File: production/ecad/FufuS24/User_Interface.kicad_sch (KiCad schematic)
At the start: 20 parts, among them J3 HDMI_A, J4 USB_B_Micro

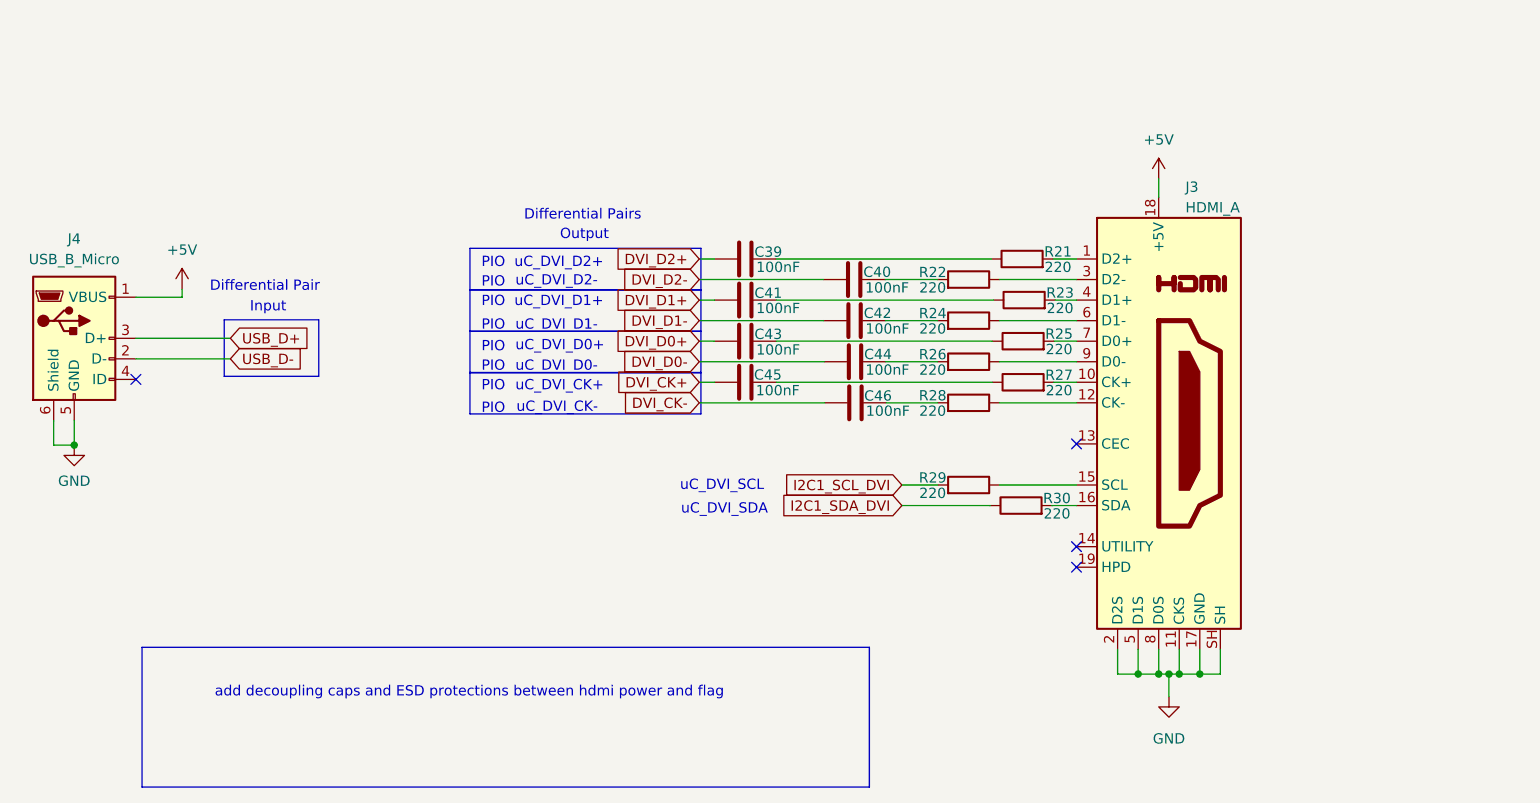
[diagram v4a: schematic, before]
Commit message: Added ESD diodes to UI schem
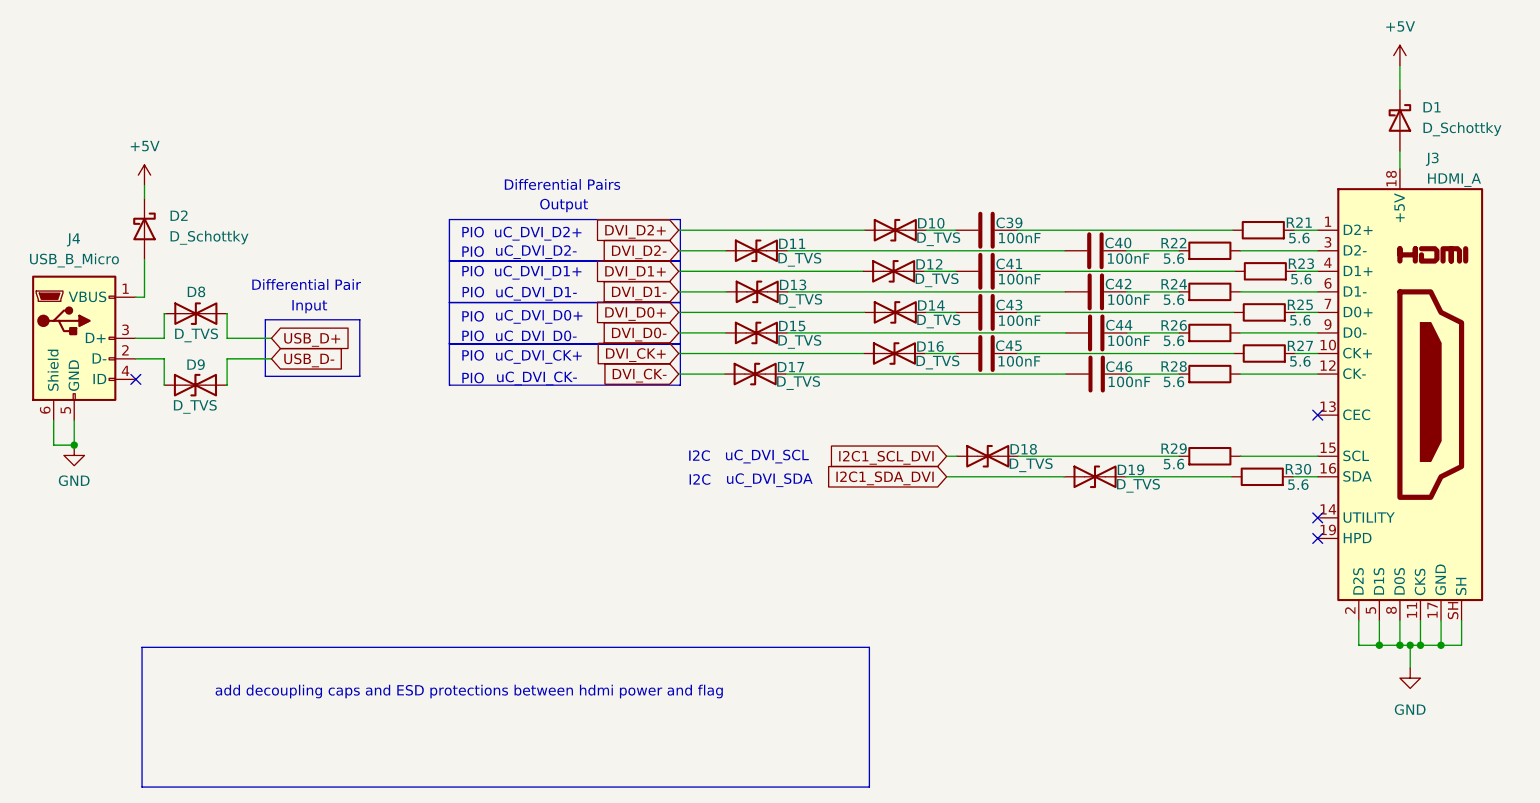
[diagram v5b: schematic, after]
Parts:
- added D1, D2: D_Schottky, symbol Device:D_Schottky
- added D10, D11, D12, D13, D14, D15, D16, D17, D18, D19, D8, D9: D_TVS, symbol Device:D_TVS
- R21, R22, R23, R24, R25, R26, R27, R28, R29, R30: value 220 -> 5.6
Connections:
- net +5V: now also D1.1 (K), D2.1 (K); no longer J3.18 (+5V), J4.1 (VBUS)
- net DVI_CK+: now also D16.1 (A1); no longer C45.1
- net DVI_CK-: now also D17.1 (A1); no longer C46.1
- net DVI_D0+: now also D14.1 (A1); no longer C43.1
- net DVI_D0-: now also D15.1 (A1); no longer C44.1
- net DVI_D1+: now also D12.1 (A1); no longer C41.1
- net DVI_D1-: now also D13.1 (A1); no longer C42.1
- net DVI_D2+: now also D10.1 (A1); no longer C39.1
- net DVI_D2-: now also D11.1 (A1); no longer C40.1
- net I2C1_SCL_DVI: now also D18.1 (A1); no longer R29.2
- net I2C1_SDA_DVI: now also D19.1 (A1); no longer R30.1
- net USB_D+: now also D8.2 (A2); no longer J4.3 (D+)
- net USB_D-: now also D9.2 (A2); no longer J4.2 (D-)
- new net: C45.1, D16.2 (A2)
- new net: C39.1, D10.2 (A2)
- new net: C41.1, D12.2 (A2)
- new net: C40.1, D11.2 (A2)
- new net: D9.1 (A1), J4.2 (D-)
- new net: D2.2 (A), J4.1 (VBUS)
- new net: D8.1 (A1), J4.3 (D+)
- new net: C44.1, D15.2 (A2)
- new net: D18.2 (A2), R29.2
- new net: C42.1, D13.2 (A2)
- new net: D1.2 (A), J3.18 (+5V)
- new net: C46.1, D17.2 (A2)
- new net: D19.2 (A2), R30.1
- new net: C43.1, D14.2 (A2)
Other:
- note added: "I2C"
- moved on the sheet: C39, C40, C41, C42, C43, C44, C45, C46, J3, R21, R22, R23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

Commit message: added ESD and diodes but idk if correctly done
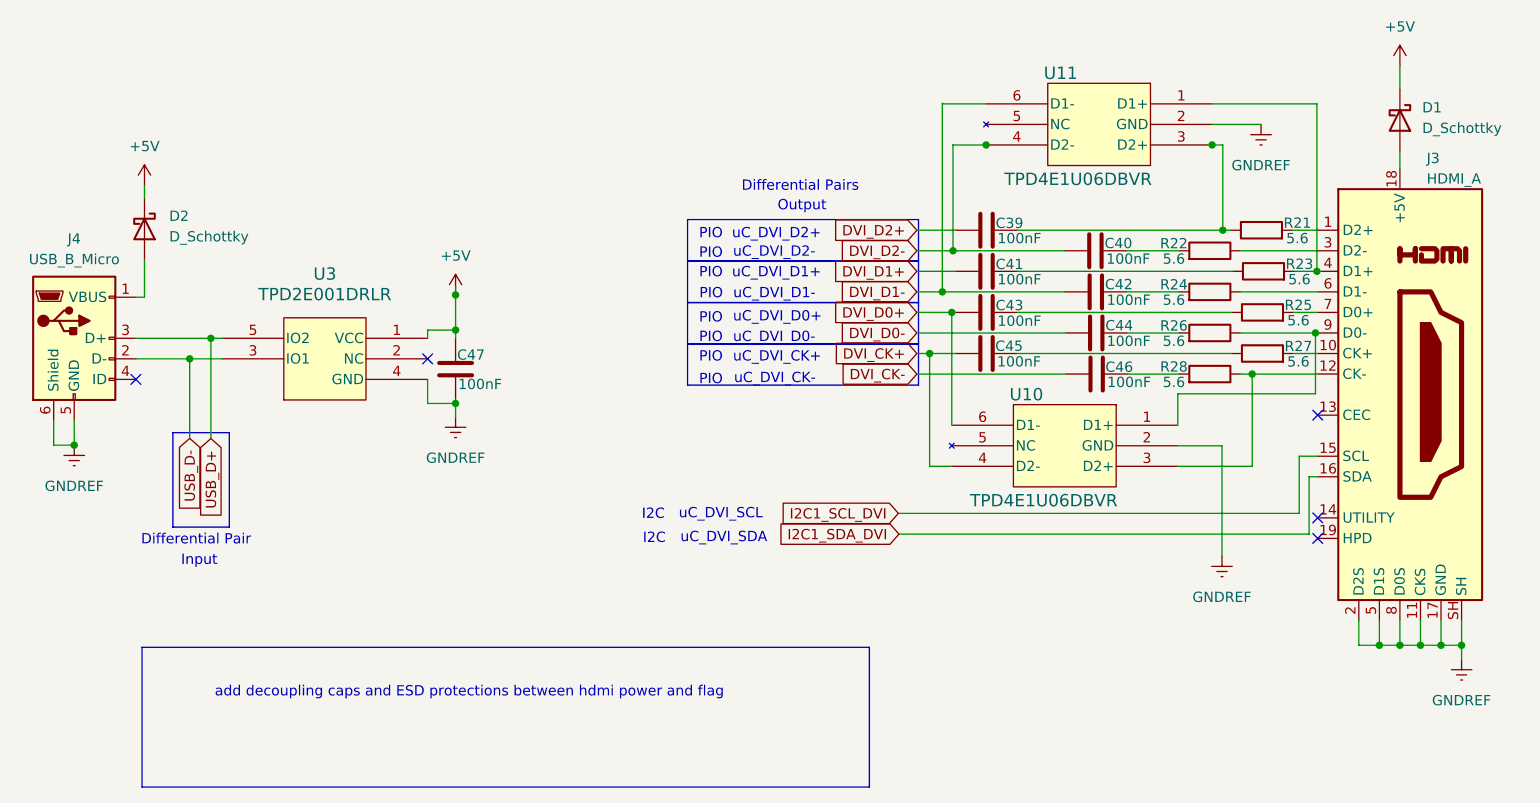
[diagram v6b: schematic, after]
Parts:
- removed D10, D11, D12, D13, D14, D15, D16, D17, D18, D19, D8, D9: D_TVS, symbol Device:D_TVS
- removed R29, R30: 5.6, symbol Device:R
- added C47: 100nF, symbol Device:C
- added U10, U11: TPD4E1U06DBVR, DBV6_TEX, symbol TPD4E1U06DBVR:TPD4E1U06DBVR
- added U3: TPD2E001DRLR, DRL5, symbol TPD2E001DRLR:TPD2E001DRLR
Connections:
- net +5V: now also C47.2, U3.1 (VCC)
- net DVI_CK+: now also C45.1, U10.4 (D2-)
- net DVI_CK-: now also C46.1
- net DVI_D0+: now also C43.1, U10.6 (D1-)
- net DVI_D0-: now also C44.1
- net DVI_D1+: now also C41.1
- net DVI_D1-: now also C42.1, U11.6 (D1-)
- net DVI_D2+: now also C39.1
- net DVI_D2-: now also C40.1, U11.4 (D2-)
- net I2C1_SCL_DVI: now also J3.15 (SCL)
- net I2C1_SDA_DVI: now also J3.16 (SDA)
- net USB_D+: now also J4.3 (D+), U3.5 (IO2)
- net USB_D-: now also J4.2 (D-), U3.3 (IO1)
- net at C39.2, R21.1: now also U11.3 (D2+)
- net at J3.12 (CK-), R28.1: now also U10.3 (D2+)
- net at J3.4 (D1+), R23.2: now also U11.1 (D1+)
- net at J3.9 (D0-), R26.1: now also U10.1 (D1+)
- net GND renamed GNDREF
- net GNDREF: now also C47.1, U10.2 (GND), U11.2 (GND), U3.4 (GND)
- no-connect marks 4 -> 5

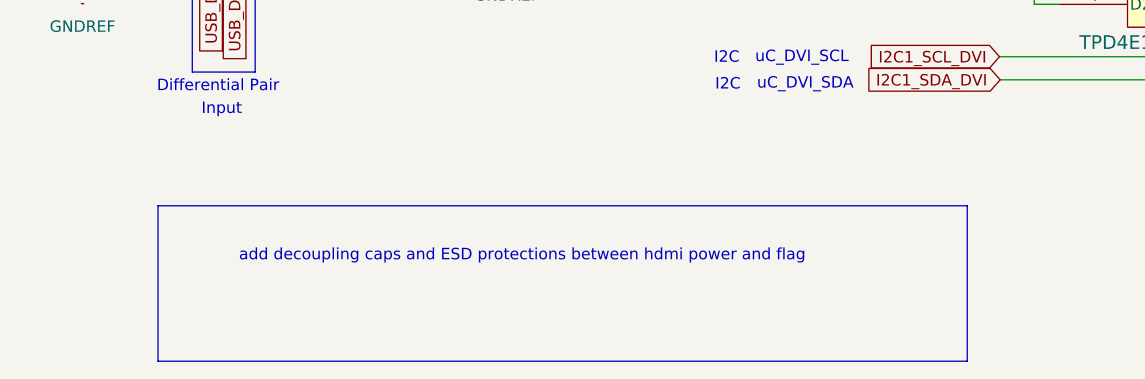
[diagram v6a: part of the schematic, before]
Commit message: removed notes from UI schem
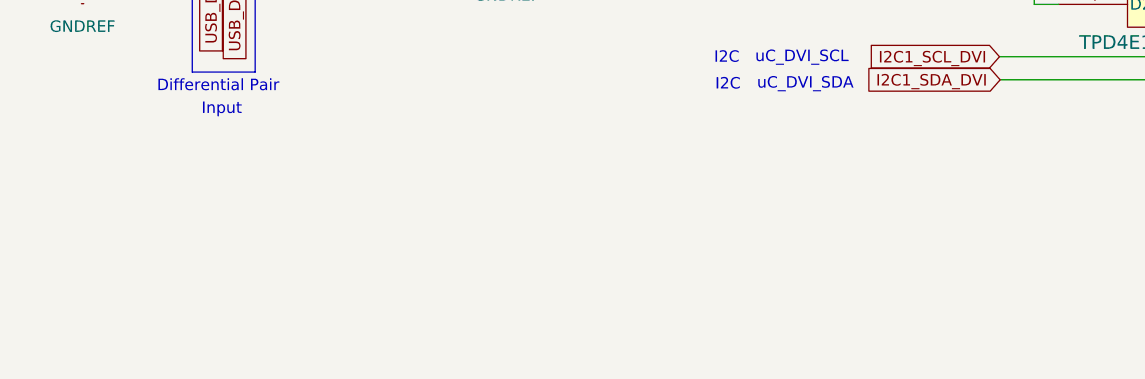
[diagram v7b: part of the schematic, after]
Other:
- note removed: "add decoupling caps and ESD protections between hdmi power and flag"
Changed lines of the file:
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@@
-    (fill (type none))
-  )
-  (rectangle (start 93.0656 107.0864) (end 182.9816 124.3584)
-    (stroke (width 0) (type default))
     (fill (type none))
   )
@@
     (effects (font (size 1.27 1.27) (color 238 64 255 1)) (justify left bottom))
   )
-  (text "add decoupling caps and ESD protections between hdmi power and flag"
-    (at 102.0572 113.4364 0)
-    (effects (font (size 1.27 1.27) (color 0 0 0 1)) (justify left bottom))
-  )
   (text "Input\n" (at 97.8916 97.1804 0)

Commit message: efan 3
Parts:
- C39, C40, C41, C42, C43, C44, C45, C46, C47: footprint (none) -> footprints:CAPC2012X94N
- R21, R22, R23, R24, R25, R26, R27, R28: footprint (none) -> footprints:RESC2012X60N
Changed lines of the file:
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@@
       (effects (font (size 1.27 1.27)))
     )
-    (property "Footprint" "" (at 231.5718 72.5424 90)
+    (property "Footprint" "footprints:RESC2012X60N" (at 231.5718 72.5424 90)
       (effects (font (size 1.27 1.27)) hide)
     )
@@
       (effects (font (size 1.27 1.27)))
     )
-    (property "Footprint" "" (at 130.8608 68.8848 0)
+    (property "Footprint" "footprints:CAPC2012X94N" (at 130.8608 68.8848 0)
       (effects (font (size 1.27 1.27)) hide)
     )
@@
       (effects (font (size 1.27 1.27)))
     )
-    (property "Footprint" "" (at 201.2696 69.7992 0)
+    (property "Footprint" "footprints:CAPC2012X94N" (at 201.2696 69.7992 0)
       (effects (font (size 1.27 1.27)) hide)
     )
@@
       (effects (font (size 1.27 1.27)))
     )
-    (property "Footprint" "" (at 214.7316 57.0992 0)
+    (property "Footprint" "footprints:CAPC2012X94N" (at 214.7316 57.0992 0)
       (effects (font (size 1.27 1.27)) hide)
     )
@@
       (effects (font (size 1.27 1.27)))
     )
-    (property "Footprint" "" (at 225.0694 59.8424 90)
+    (property "Footprint" "footprints:RESC2012X60N" (at 225.0694 59.8424 90)
       (effects (font (size 1.27 1.27)) hide)
     )
@@
       (effects (font (size 1.27 1.27)))
     )
-    (property "Footprint" "" (at 225.0694 64.9224 90)
+    (property "Footprint" "footprints:RESC2012X60N" (at 225.0694 64.9224 90)
       (effects (font (size 1.27 1.27)) hide)
     )
@@
       (effects (font (size 1.27 1.27)))
     )
-    (property "Footprint" "" (at 201.2696 54.5592 0)
+    (property "Footprint" "footprints:CAPC2012X94N" (at 201.2696 54.5592 0)
       (effects (font (size 1.27 1.27)) hide)
     )
@@
       (effects (font (size 1.27 1.27)))
     )
-    (property "Footprint" "" (at 231.4448 57.3024 90)
+    (property "Footprint" "footprints:RESC2012X60N" (at 231.4448 57.3024 90)
       (effects (font (size 1.27 1.27)) hide)
     )
@@
       (effects (font (size 1.27 1.27)))
     )
-    (property "Footprint" "" (at 214.8332 67.2592 0)
+    (property "Footprint" "footprints:CAPC2012X94N" (at 214.8332 67.2592 0)
       (effects (font (size 1.27 1.27)) hide)
     )
@@
       (effects (font (size 1.27 1.27)))
     )
-    (property "Footprint" "" (at 214.7824 62.1792 0)
+    (property "Footprint" "footprints:CAPC2012X94N" (at 214.7824 62.1792 0)
       (effects (font (size 1.27 1.27)) hide)
     )
@@
       (effects (font (size 1.27 1.27)))
     )
-    (property "Footprint" "" (at 231.6988 62.3824 90)
+    (property "Footprint" "footprints:RESC2012X60N" (at 231.6988 62.3824 90)
       (effects (font (size 1.27 1.27)) hide)
     )
@@
       (effects (font (size 1.27 1.27)))
     )
-    (property "Footprint" "" (at 225.0694 75.0824 90)
+    (property "Footprint" "footprints:RESC2012X60N" (at 225.0694 75.0824 90)
       (effects (font (size 1.27 1.27)) hide)
     )
@@
       (effects (font (size 1.27 1.27)))
     )
-    (property "Footprint" "" (at 214.884 72.3392 0)
+    (property "Footprint" "footprints:CAPC2012X94N" (at 214.884 72.3392 0)
       (effects (font (size 1.27 1.27)) hide)
     )
@@
       (effects (font (size 1.27 1.27)))
     )
-    (property "Footprint" "" (at 231.5718 67.4624 90)
+    (property "Footprint" "footprints:RESC2012X60N" (at 231.5718 67.4624 90)
       (effects (font (size 1.27 1.27)) hide)
     )
@@
       (effects (font (size 1.27 1.27)))
     )
-    (property "Footprint" "" (at 225.0694 70.0024 90)
+    (property "Footprint" "footprints:RESC2012X60N" (at 225.0694 70.0024 90)
       (effects (font (size 1.27 1.27)) hide)
     )
@@
       (effects (font (size 1.27 1.27)))
     )
-    (property "Footprint" "" (at 201.2696 59.6392 0)
+    (property "Footprint" "footprints:CAPC2012X94N" (at 201.2696 59.6392 0)
       (effects (font (size 1.27 1.27)) hide)
     )
@@
       (effects (font (size 1.27 1.27)))
     )
-    (property "Footprint" "" (at 201.2696 64.7192 0)
-      (effects (font (size 1.27 1.27)) hide)
-    )
+    (property "Footprint" "footprints:CAPC2012X94N" (at 201.2696 64.7192 0)
+      (effects (font (size 1.27 1.27)) hide)
+    )
